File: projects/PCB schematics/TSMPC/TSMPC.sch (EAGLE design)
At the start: 16 parts, among them X1 AS06-05

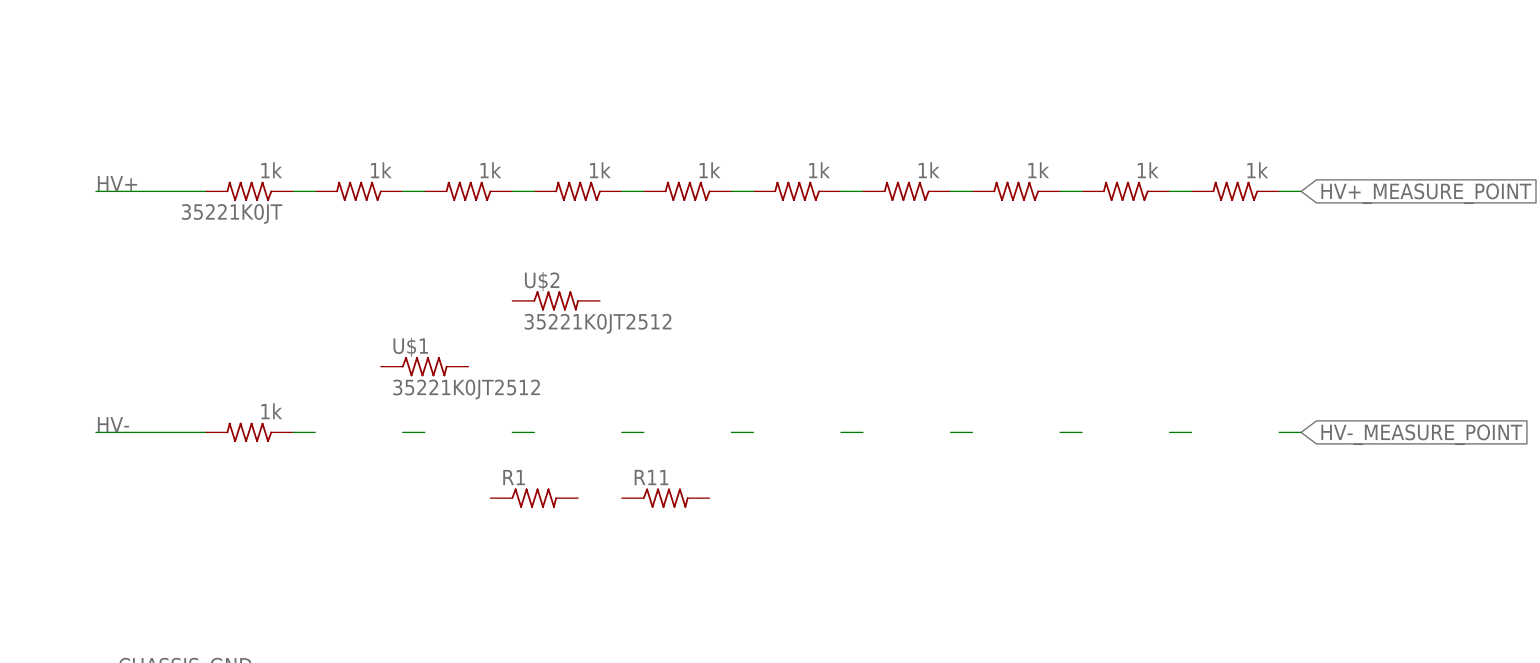
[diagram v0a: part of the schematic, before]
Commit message: TSMPC - Initial revision.
Completed board, minus the connector. Still needs verification from @michaelpass .
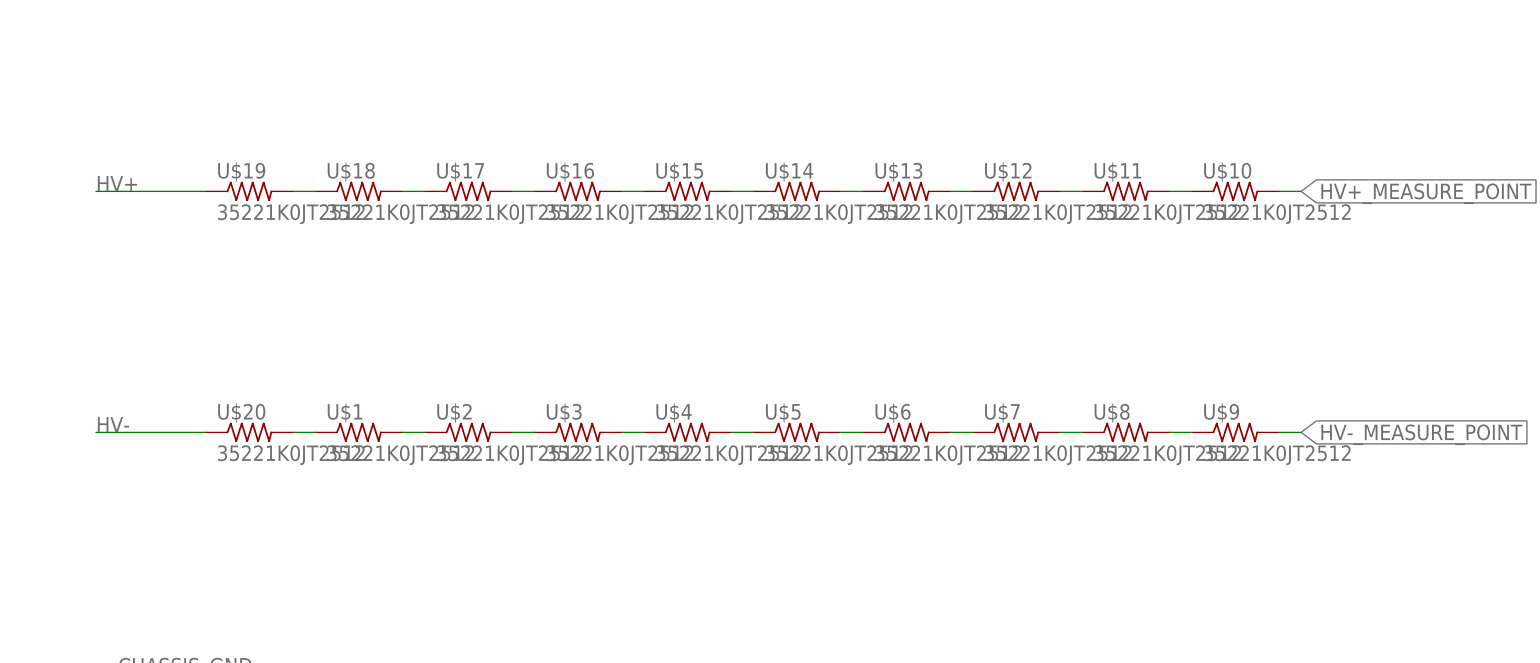
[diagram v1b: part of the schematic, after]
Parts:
- removed 35221K0JT, R10, R2, R3, R4, R5, R6, R7, R8, R9: 1k, rcl:R-US_R0805
- removed R1, R11: (no value), rcl:R-US_R0805
- removed R21: 1k, rcl:R-US_R2512
- added U$10, U$11, U$12, U$13, U$14, U$15, U$16, U$17, U$18, U$19, U$20, U$3, U$4, U$5, U$6, U$7, U$8, U$9: 35221K0JT2512, IowaFormula:35221K0JT2512
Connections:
- new net N$22: U$1.2, U$2.1
- new net N$23: U$2.2, U$3.1
- new net N$24: U$3.2, U$4.1
- new net N$25: U$4.2, U$5.1
- new net N$26: U$5.2, U$6.1
- new net N$27: U$6.2, U$7.1
- new net N$28: U$7.2, U$8.1
- new net N$29: U$8.2, U$9.1
- net HV+: now also U$19.1; no longer 35221K0JT.2
- net HV+_MEASURE_POINT: now also U$10.2; no longer R10.1
- net HV-: now also U$20.1; no longer R21.2
- net HV-_MEASURE_POINT: now also U$9.2
- net N$1: now also U$18.1, U$19.2; no longer 35221K0JT.1, R2.2
- net N$2: now also U$17.1, U$18.2; no longer R2.1, R3.2
- net N$21: now also U$1.1, U$20.2; no longer R21.1
- net N$3: now also U$16.1, U$17.2; no longer R3.1, R4.2
- net N$4: now also U$15.1, U$16.2; no longer R4.1, R5.2
- net N$5: now also U$14.1, U$15.2; no longer R5.1, R6.2
- net N$6: now also U$13.1, U$14.2; no longer R6.1, R7.2
- net N$7: now also U$12.1, U$13.2; no longer R7.1, R8.2
- net N$8: now also U$11.1, U$12.2; no longer R8.1, R9.2
- net N$9: now also U$10.1, U$11.2; no longer R10.2, R9.1
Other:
- moved on the sheet: U$1, U$2

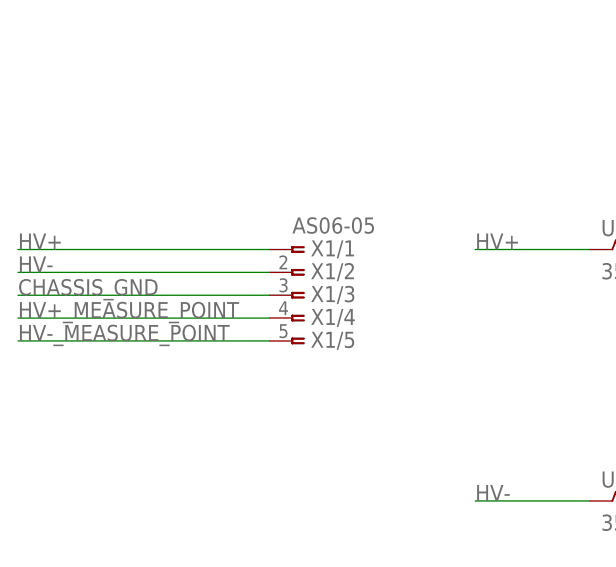
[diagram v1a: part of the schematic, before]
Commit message: TSMPC - Initial revisions from pull request #3.
Many changes were needed from Anshuman's initial pull request version. Half of the necessary changes have been made here. Connectors must be added. I believe we should also add in a seperate GND board and not have our chassis point on this board, so as to avoid potential isolation issues.
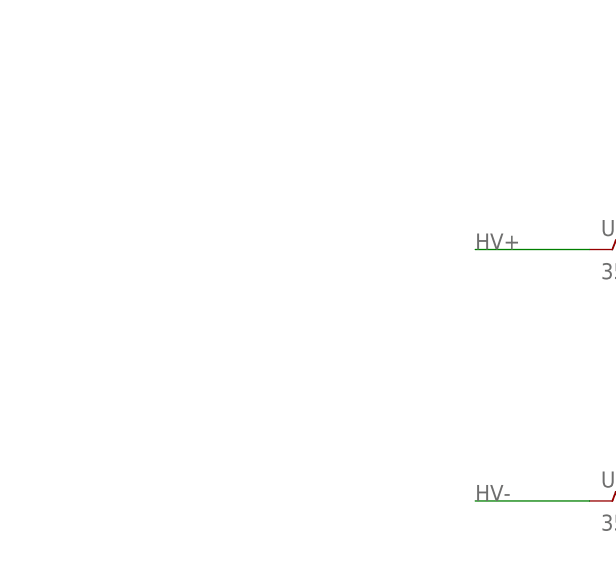
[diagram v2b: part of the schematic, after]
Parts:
- removed X1: AS06-05, con-deutsch:AS06-05
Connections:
- removed net CHASSIS_GND: X1/3.1
- net HV+: no longer X1/1.1
- net HV+_MEASURE_POINT: no longer X1/4.1
- net HV-: no longer X1/2.1
- net HV-_MEASURE_POINT: no longer X1/5.1
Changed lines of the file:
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@@
 <part name="FRAME2" library="frames" library_urn="urn:adsk.eagle:library:229" deviceset="FRAME_A_L" device=""/>
 <part name="GND2" library="supply1" library_urn="urn:adsk.eagle:library:371" deviceset="GND" device=""/>
-<part name="X1" library="con-deutsch" library_urn="urn:adsk.eagle:library:139" deviceset="AS06-05" device="" package3d_urn="urn:adsk.eagle:package:6519/1"/>
 <part name="U$1" library="IowaFormula" deviceset="35221K0JT" device="2512" package3d_urn="urn:adsk.eagle:package:23545/2"/>
 <part name="U$2" library="IowaFormula" deviceset="35221K0JT" device="2512" package3d_urn="urn:adsk.eagle:package:23545/2"/>
@@
 <attribute name="VALUE" x="7.62" y="5.08" size="1.778" layer="96"/>
 </instance>
-<instance part="X1" gate="/1" x="-12.7" y="71.12" smashed="yes">
-<attribute name="NAME" x="-10.668" y="70.358" size="1.778" layer="95"/>
-<attribute name="VALUE" x="-12.7" y="72.898" size="1.778" layer="96"/>
-</instance>
-<instance part="X1" gate="/2" x="-12.7" y="68.58" smashed="yes">
-<attribute name="NAME" x="-10.668" y="67.818" size="1.778" layer="95"/>
-</instance>
-<instance part="X1" gate="/3" x="-12.7" y="66.04" smashed="yes">
-<attribute name="NAME" x="-10.668" y="65.278" size="1.778" layer="95"/>
-</instance>
-<instance part="X1" gate="/4" x="-12.7" y="63.5" smashed="yes">
-<attribute name="NAME" x="-10.668" y="62.738" size="1.778" layer="95"/>
-</instance>
-<instance part="X1" gate="/5" x="-12.7" y="60.96" smashed="yes">
-<attribute name="NAME" x="-10.668" y="60.198" size="1.778" layer="95"/>
-</instance>
 <instance part="U$1" gate="G$1" x="38.1" y="43.18" smashed="yes">
 <attribute name="NAME" x="34.29" y="44.6786" size="1.778" layer="95"/>
@@
 <pinref part="U$10" gate="G$1" pin="2"/>
 </segment>
-<segment>
-<pinref part="X1" gate="/4" pin="1"/>
-<label x="-43.18" y="63.5" size="1.778" layer="255"/>
-<wire x1="-15.24" y1="63.5" x2="-43.18" y2="63.5" width="0.1524" layer="91"/>
-</segment>
 </net>
 <net name="N$21" class="0">
@@
 <pinref part="U$9" gate="G$1" pin="2"/>
 </segment>
-<segment>
-<pinref part="X1" gate="/5" pin="1"/>
-<wire x1="-15.24" y1="60.96" x2="-43.18" y2="60.96" width="0.1524" layer="91"/>
-<label x="-43.18" y="60.96" size="1.778" layer="255"/>
-</segment>
 </net>
 <net name="HV+" class="0">
-<segment>
-<pinref part="X1" gate="/1" pin="1"/>
-<wire x1="-15.24" y1="71.12" x2="-43.18" y2="71.12" width="0.1524" layer="91"/>
-<label x="-43.18" y="71.12" size="1.778" layer="95"/>
-</segment>
 <segment>
 <wire x1="20.32" y1="71.12" x2="7.62" y2="71.12" width="0.1524" layer="91"/>
@@
 </net>
 <net name="HV-" class="0">
-<segment>
-<wire x1="-15.24" y1="68.58" x2="-43.18" y2="68.58" width="0.1524" layer="91"/>
-<pinref part="X1" gate="/2" pin="1"/>
-<label x="-43.18" y="68.58" size="1.778" layer="95"/>
-</segment>
 <segment>
 <wire x1="20.32" y1="43.18" x2="7.62" y2="43.18" width="0.1524" layer="91"/>
@@
 <label x="10.16" y="15.24" size="1.778" layer="255"/>
 </segment>
-<segment>
-<wire x1="-15.24" y1="66.04" x2="-43.18" y2="66.04" width="0.1524" layer="91"/>
-<pinref part="X1" gate="/3" pin="1"/>
-<label x="-43.18" y="66.04" size="1.778" layer="95"/>
-</segment>
-</net>
+</net>

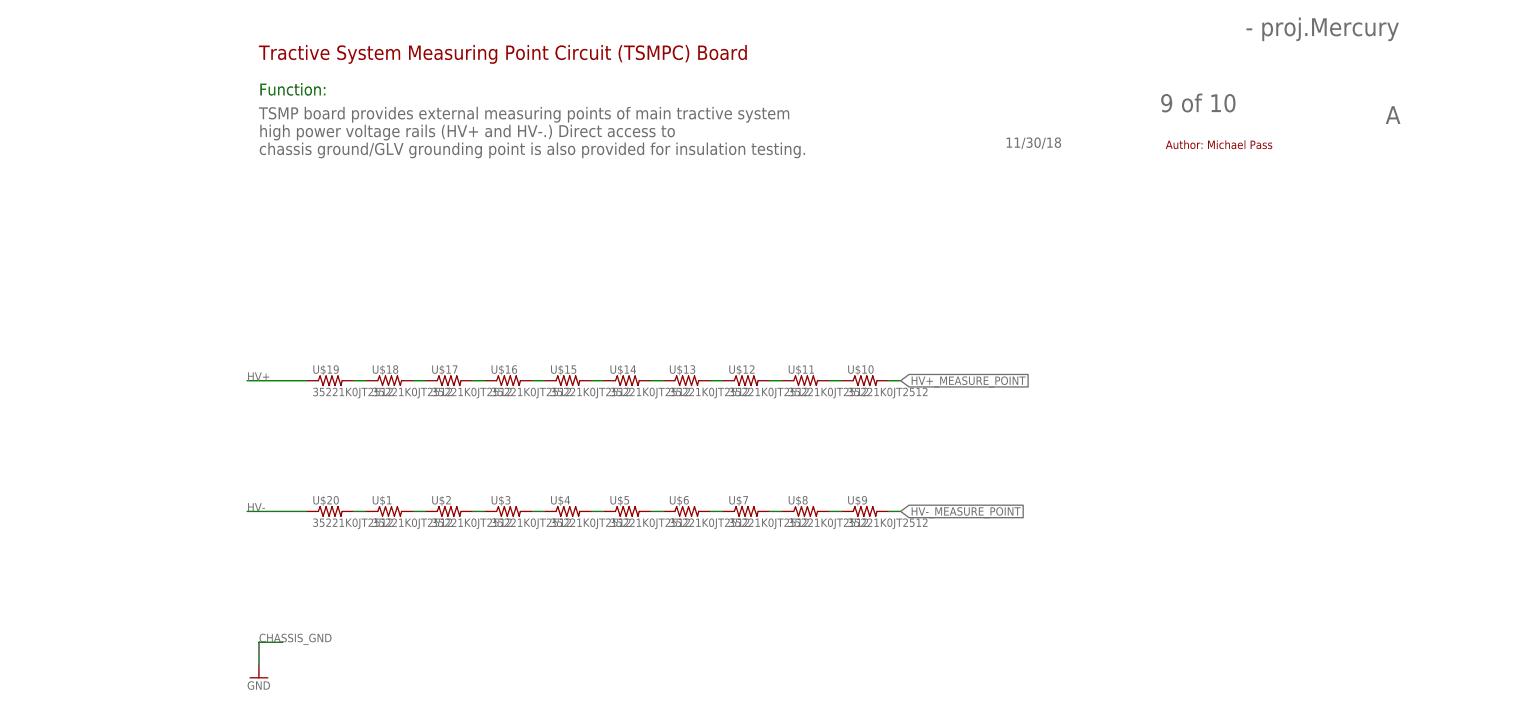
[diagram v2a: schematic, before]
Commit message: TSMPC - Additional revisions for pull request #3.
Final revisions (apart from connectors and creation of simple GND board) have been done and are ready for review by Anshuman Sahu (and selection of HV connectors)

Squash - TSMPC - Fixed missing connection as per @rgoedken, PR#3.

Squash - TSMPC - Added connectors. PR#3 suggestions. Pending approval.
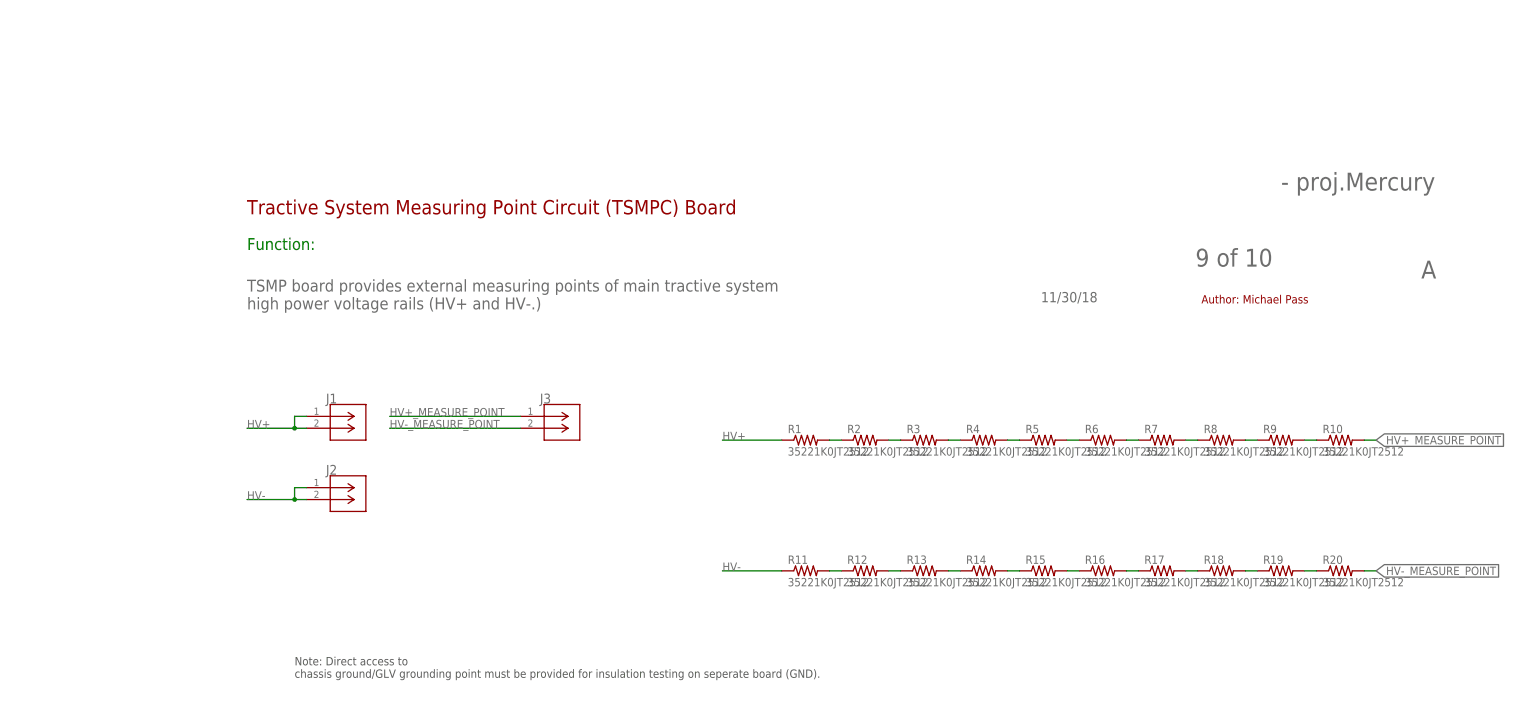
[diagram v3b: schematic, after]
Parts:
- removed U$1, U$10, U$11, U$12, U$13, U$14, U$15, U$16, U$17, U$18, U$19, U$2, U$20, U$3, U$4, U$5, U$6, U$7, U$8, U$9: 35221K0JT2512, IowaFormula:35221K0JT2512
- added J1, J2, J3: 2P_1-770166-0, con-MATE-N-LOK:2P_1-770166-0
- added R1, R10, R11, R12, R13, R14, R15, R16, R17, R18, R19, R2, R20, R3, R4, R5, R6, R7, R8, R9: 35221K0JT2512, IowaFormula:35221K0JT2512
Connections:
- net HV+: now also J1.1, J1.2, R1.1; no longer U$19.1
- net HV+_MEASURE_POINT: now also J3.1, R10.2; no longer U$10.2
- net HV-: now also J2.1, J2.2, R11.1; no longer U$20.1
- net HV-_MEASURE_POINT: now also J3.2, R20.2; no longer U$9.2
- net N$1: now also R1.2, R2.1; no longer U$18.1, U$19.2
- net N$2: now also R2.2, R3.1; no longer U$17.1, U$18.2
- net N$21: now also R11.2, R12.1; no longer U$1.1, U$20.2
- net N$22: now also R12.2, R13.1; no longer U$1.2, U$2.1
- net N$23: now also R13.2, R14.1; no longer U$2.2, U$3.1
- net N$24: now also R14.2, R15.1; no longer U$3.2, U$4.1
- net N$25: now also R15.2, R16.1; no longer U$4.2, U$5.1
- net N$26: now also R16.2, R17.1; no longer U$5.2, U$6.1
- net N$27: now also R17.2, R18.1; no longer U$6.2, U$7.1
- net N$28: now also R18.2, R19.1; no longer U$7.2, U$8.1
- net N$29: now also R19.2, R20.1; no longer U$8.2, U$9.1
- net N$3: now also R3.2, R4.1; no longer U$16.1, U$17.2
- net N$4: now also R4.2, R5.1; no longer U$15.1, U$16.2
- net N$5: now also R5.2, R6.1; no longer U$14.1, U$15.2
- net N$6: now also R6.2, R7.1; no longer U$13.1, U$14.2
- net N$7: now also R7.2, R8.1; no longer U$12.1, U$13.2
- net N$8: now also R8.2, R9.1; no longer U$11.1, U$12.2
- net N$9: now also R10.1, R9.2; no longer U$10.1, U$11.2
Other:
- note added: "Note: Direct access to chassis ground/GLV grounding point must be provided for insulation testing on seperate board (GND)."
- note added: "TSMP board provides external measuring points of main tractive system high power voltage rails (HV+ and HV-.)"
- note removed: "TSMP board provides external measuring points of main tractive system high power voltage rails (HV+ and HV-.) Direct access to chassis ground/GLV grounding point is also provided for insulation testing."
